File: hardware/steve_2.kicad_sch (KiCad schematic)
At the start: 32 parts, among them Q1 Q_NMOS_GSD

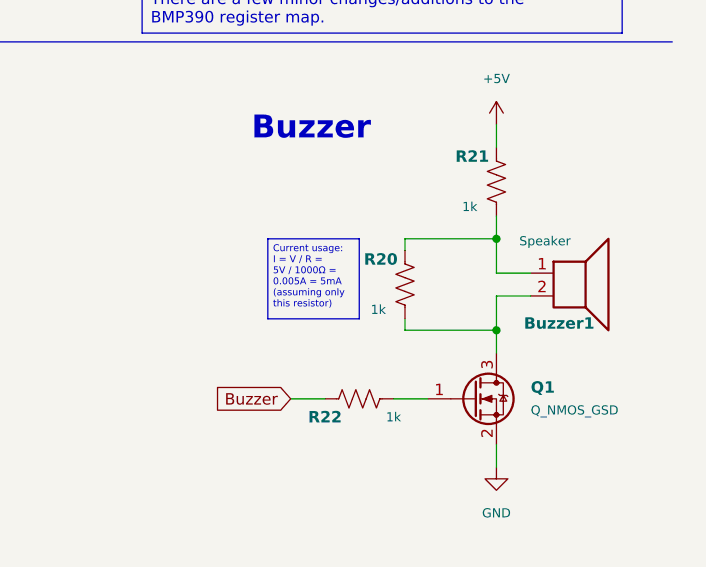
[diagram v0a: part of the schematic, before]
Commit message: Finished routing traces
Finished routing traces. Also added extra ground vias to stitch the ground planes together. Lessons for next time: power pads (on a microcontroller or other) should immediately get a via; passives can go on the back (including decoupling caps if power vias are close); everything should be spaced further; try not to put 2 unrelated components on top of each other; uC signal traces should be fanned out (mostly inwards) and via'd for ease of use
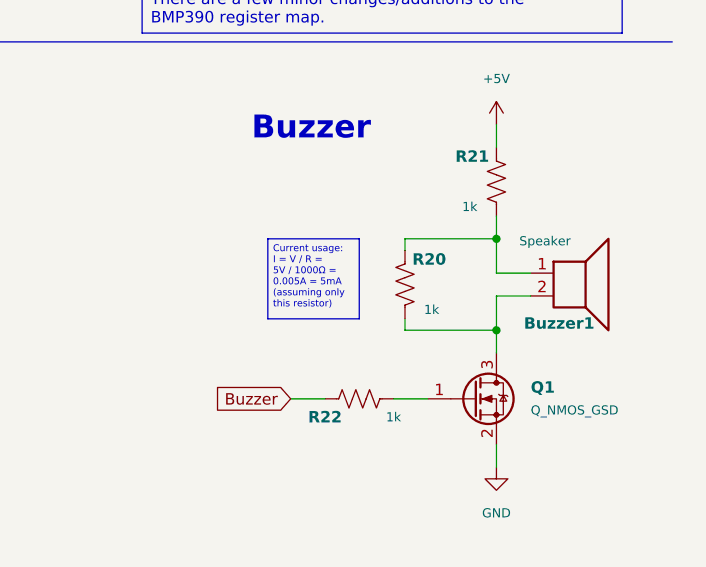
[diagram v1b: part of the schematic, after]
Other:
- moved on the sheet: R20
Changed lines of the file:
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@@
 	(symbol
 		(lib_id "Device:R_US")
-		(at 255.27 102.87 180)
+		(at 255.27 102.87 0)
+		(mirror x)
 		(unit 1)
 		(exclude_from_sim no)
@@
 		(dnp no)
 		(property "Reference" "R20"
-			(at 250.698 100.076 0)
+			(at 259.842 100.076 0)
 			(effects
 				(font
@@
 		)
 		(property "Value" "1k"
-			(at 251.46 105.664 0)
+			(at 259.08 105.664 0)
 			(effects
 				(font
@@
 		)
 		(property "Footprint" "Resistor_SMD:R_0603_1608Metric"
-			(at 254.254 102.616 90)
+			(at 256.286 102.616 90)
 			(effects
 				(font

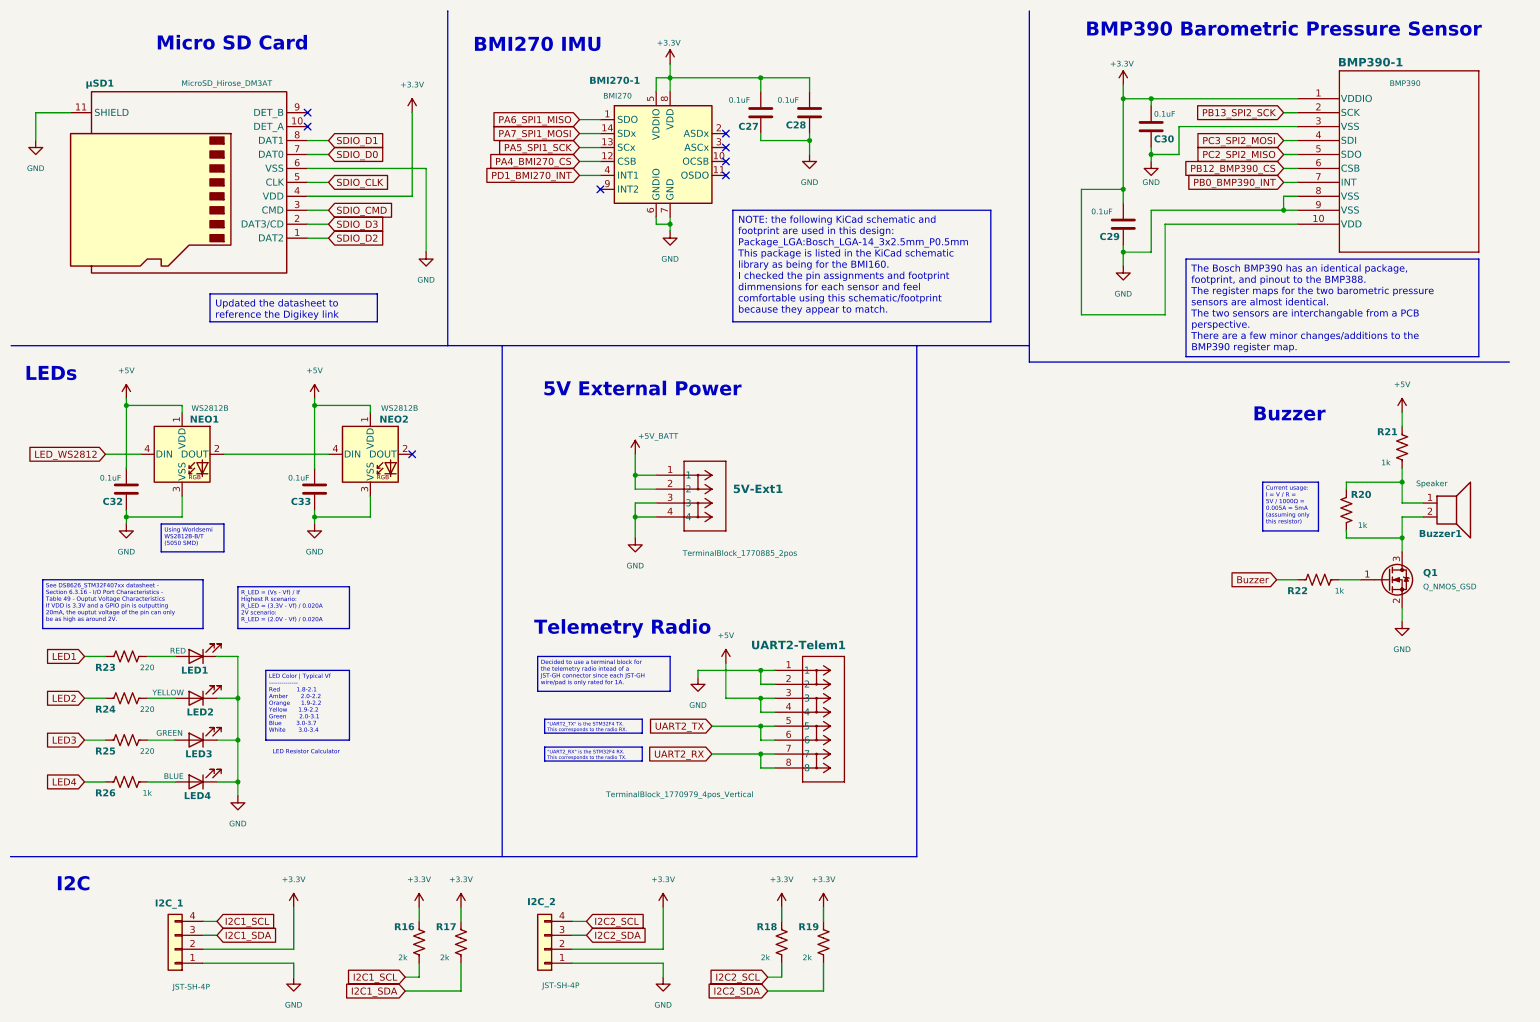
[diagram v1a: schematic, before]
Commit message: Schematic and Board fixes for Mfg
Schematic and Board fixes for Manufacturing. Added LCSC/JLC part numbers to values in schematic for BOM processing. Updated schematic fields. Added GND to each PSM connector. Brought PSM connector fix to PCB. Updated PCB designator locations from schematic changes.
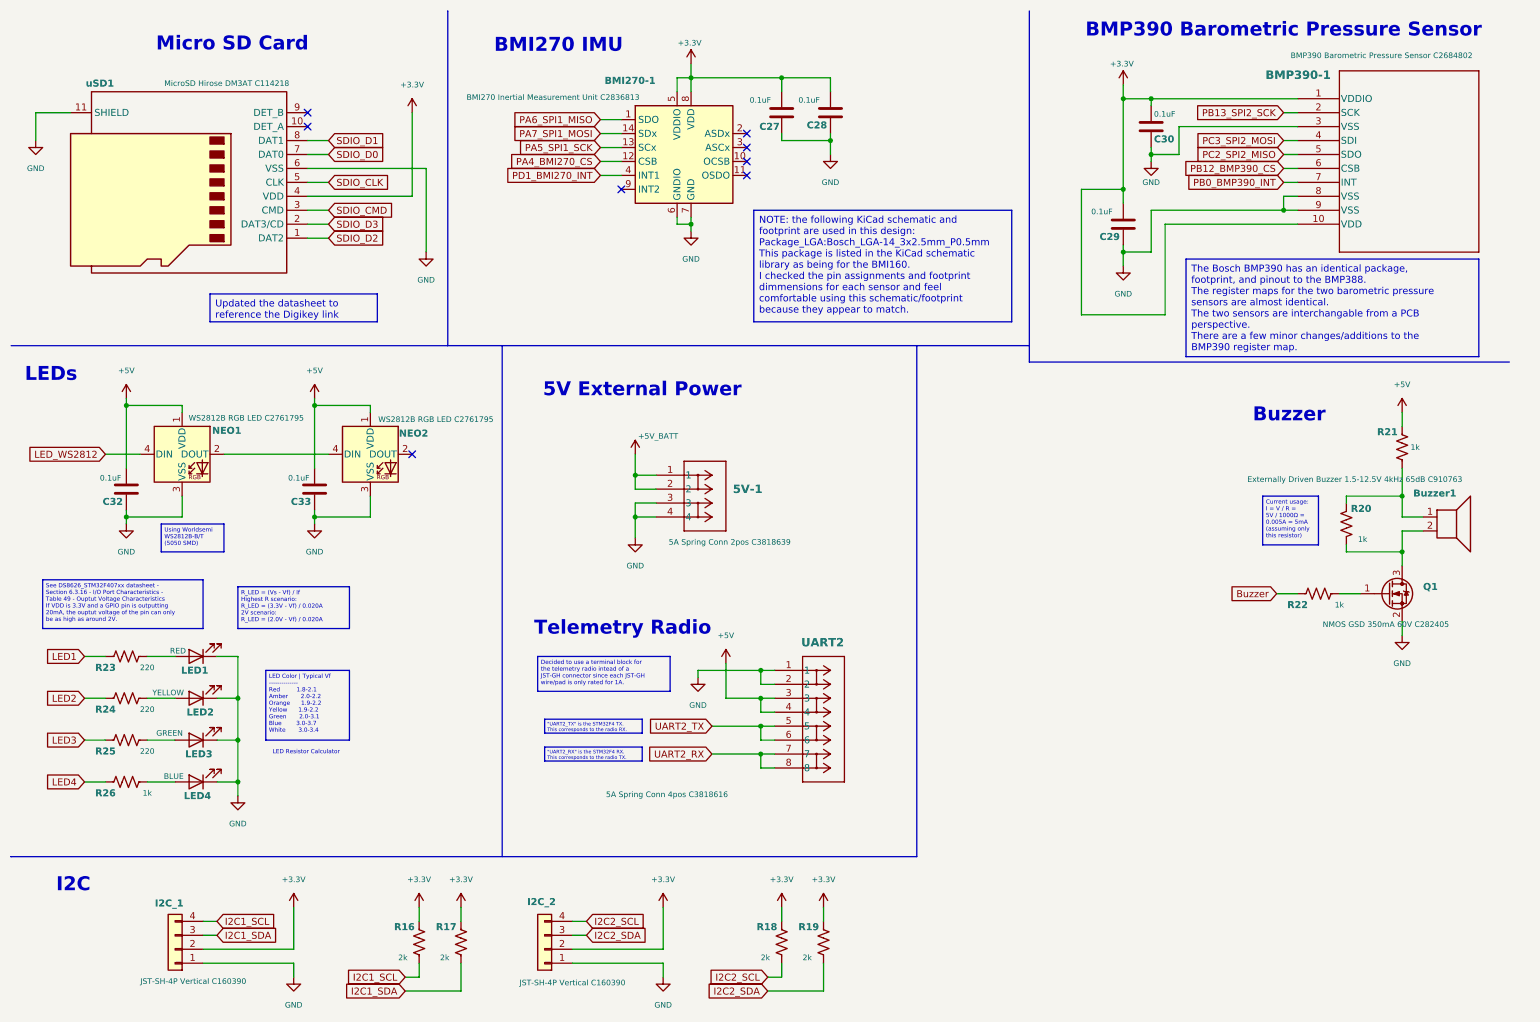
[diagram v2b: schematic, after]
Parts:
- 5V-1: renamed from 5V-Ext1; value TerminalBlock_1770885_2pos -> 5A Spring Conn 2pos C3818639
- BMI270-1: value BMI270 -> BMI270 Inertial Measurement Unit C2836813
- BMP390-1: value BMP390 -> BMP390 Barometric Pressure Sensor C2684802
- Buzzer1: value Speaker -> Externally Driven Buzzer 1.5-12.5V 4kHz 65dB C910763
- I2C_1, I2C_2: value JST-SH-4P -> JST-SH-4P Vertical C160390
- NEO1, NEO2: value WS2812B -> WS2812B RGB LED C2761795
- Q1: value Q_NMOS_GSD -> NMOS GSD 350mA 60V C282405
- UART2: renamed from UART2-Telem1; value TerminalBlock_1770979_4pos_Vertical -> 5A Spring Conn 4pos C3818616
- uSD1: renamed from µSD1; value MicroSD_Hirose_DM3AT -> MicroSD Hirose DM3AT C114218
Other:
- moved on the sheet: BMI270-1, Buzzer1, C27, C28, Q1, R20, R22

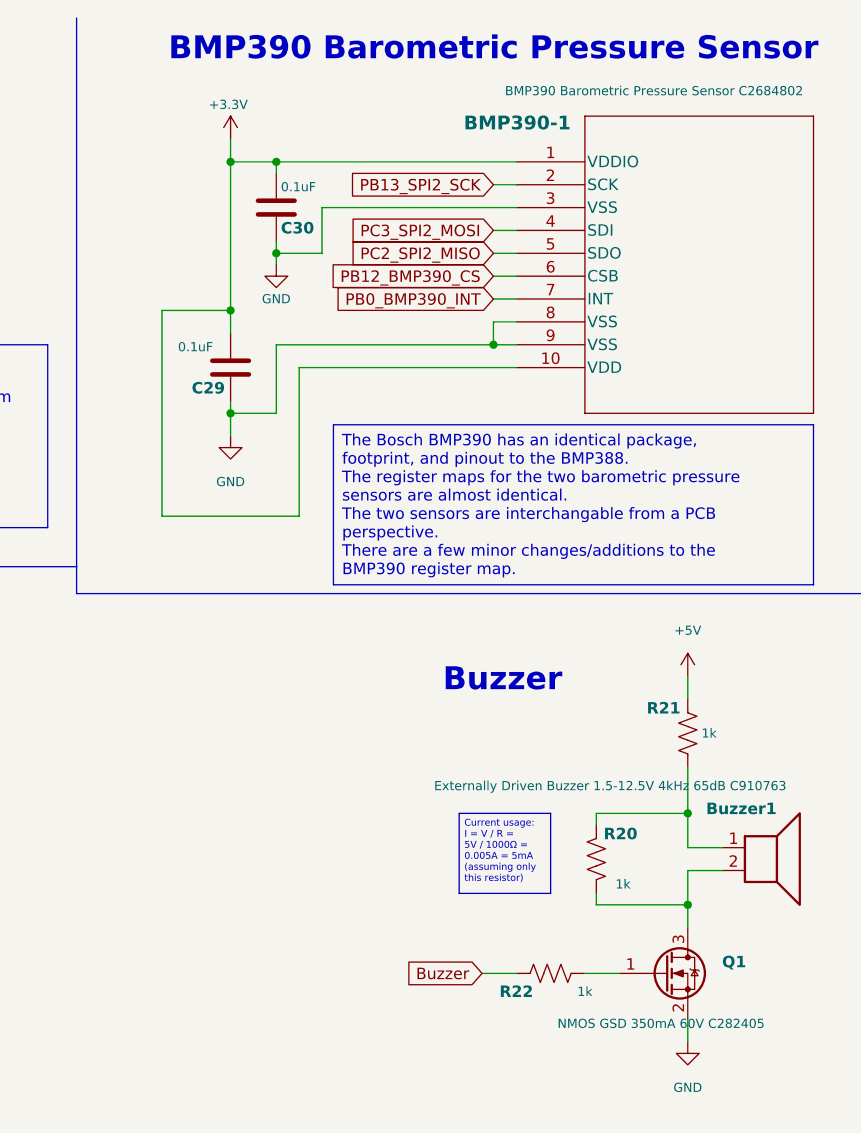
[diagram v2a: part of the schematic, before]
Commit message: Fixed all ERC issues; fixed important DRC issues
Fixed all ERC Errors and Warnings in the schematic. Fixed all Errors and Warnings in the DRC for the board (Not counting JLC 4-Wire Kelvin test and plane thermal relief spoke errors that were manually reviewed and excluded).
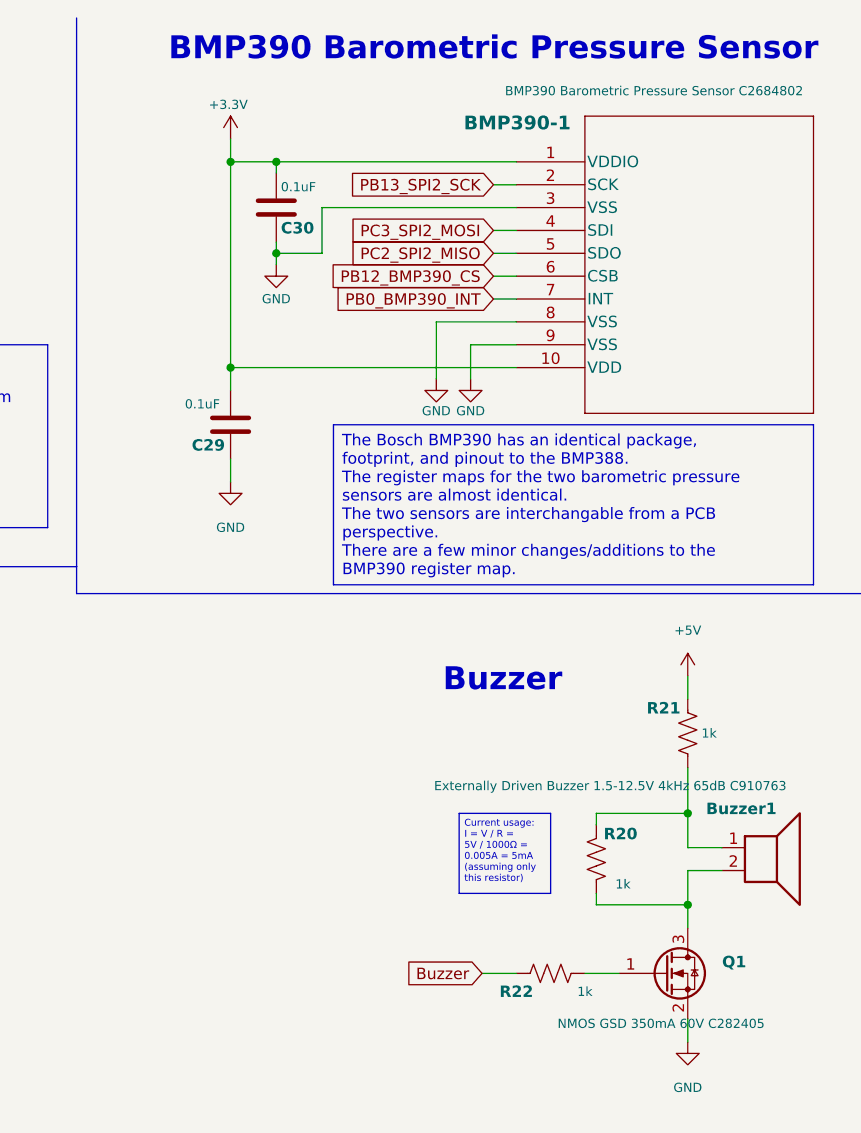
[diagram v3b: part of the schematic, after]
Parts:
- Q1: symbol Device:Q_NMOS_GSD -> Transistor_FET:Q_NMOS_GSD
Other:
- moved on the sheet: C29
